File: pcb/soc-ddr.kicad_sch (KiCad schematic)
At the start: 1 part, among them U1 XC7Z020CLG484

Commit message: hierarchy and cleaning
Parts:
- removed U1: XC7Z020CLG484, Package_BGA:Xilinx_CLG484_CLG485, symbol library:XC7Z020CLG484
- added U1: XC7Z020CLG484, Package_BGA:Xilinx_CLG484_CLG485, symbol library:XC7Z020CLG484

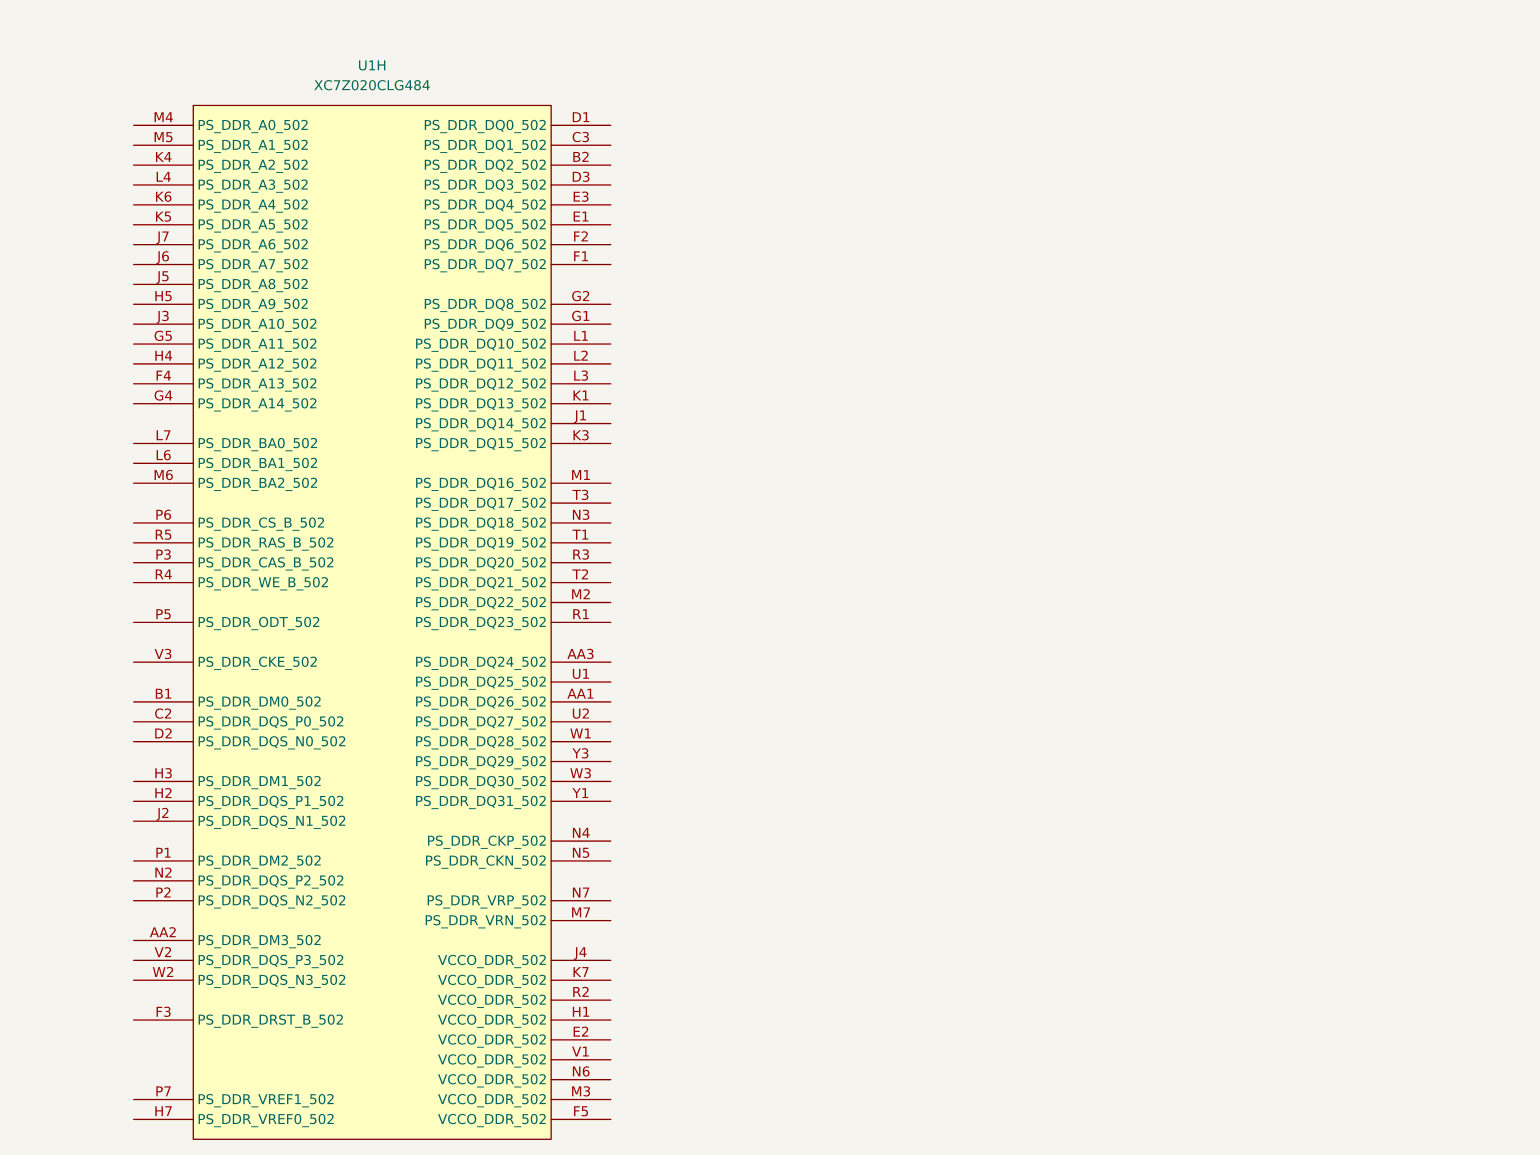
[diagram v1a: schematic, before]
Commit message: schematic structure, added qspi flash, pinout defs. mostly work on PS pinouts, defining comms. buses, still need to choose dram part, phys, camera/bus, power supply etc
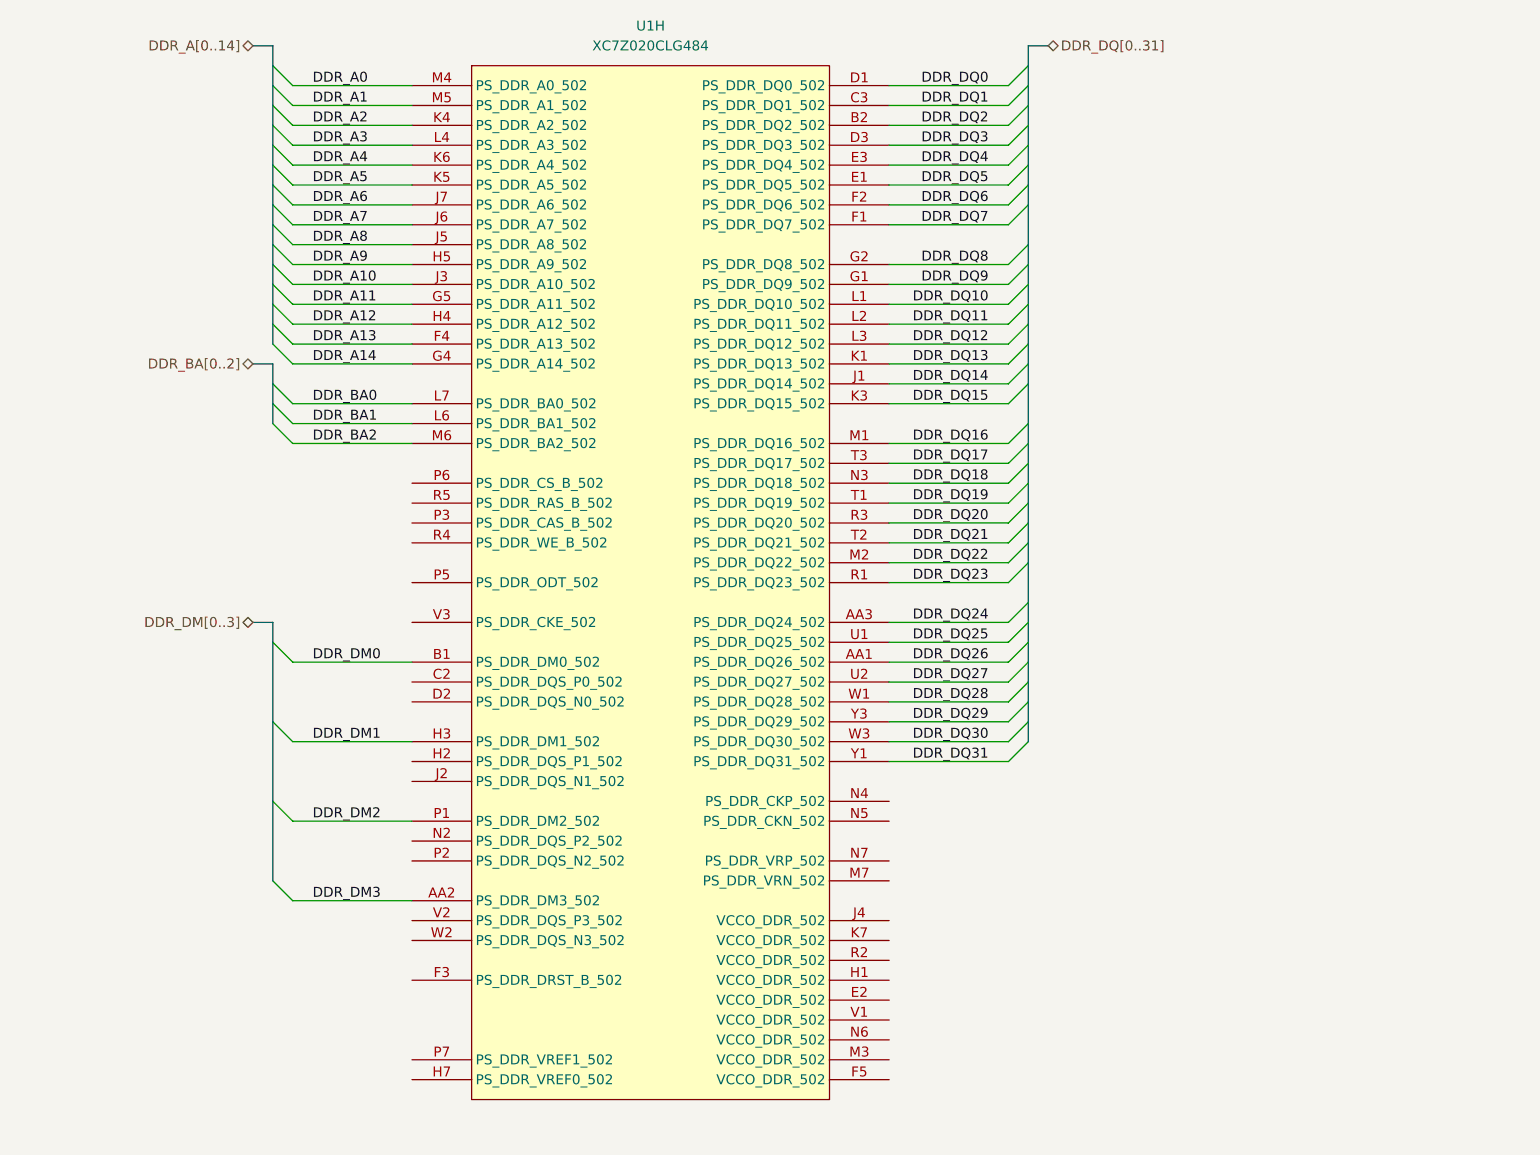
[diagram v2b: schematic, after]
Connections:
- net DDR_DQ26: now reaches U1.AA1 (PS_DDR_DQ26_502)
- net DDR_DM3: now reaches U1.AA2 (PS_DDR_DM3_502)
- net DDR_DQ24: now reaches U1.AA3 (PS_DDR_DQ24_502)
- net DDR_DM0: now reaches U1.B1 (PS_DDR_DM0_502)
- net DDR_DQ2: now reaches U1.B2 (PS_DDR_DQ2_502)
- net DDR_DQ1: now reaches U1.C3 (PS_DDR_DQ1_502)
- net DDR_DQ0: now reaches U1.D1 (PS_DDR_DQ0_502)
- net DDR_DQ3: now reaches U1.D3 (PS_DDR_DQ3_502)
- net DDR_DQ5: now reaches U1.E1 (PS_DDR_DQ5_502)
- net DDR_DQ4: now reaches U1.E3 (PS_DDR_DQ4_502)
- net DDR_DQ7: now reaches U1.F1 (PS_DDR_DQ7_502)
- net DDR_DQ6: now reaches U1.F2 (PS_DDR_DQ6_502)
- net DDR_A13: now reaches U1.F4 (PS_DDR_A13_502)
- net DDR_DQ9: now reaches U1.G1 (PS_DDR_DQ9_502)
- net DDR_DQ8: now reaches U1.G2 (PS_DDR_DQ8_502)
- net DDR_A14: now reaches U1.G4 (PS_DDR_A14_502)
- net DDR_A11: now reaches U1.G5 (PS_DDR_A11_502)
- net DDR_DM1: now reaches U1.H3 (PS_DDR_DM1_502)
- net DDR_A12: now reaches U1.H4 (PS_DDR_A12_502)
- net DDR_A9: now reaches U1.H5 (PS_DDR_A9_502)
- net DDR_DQ14: now reaches U1.J1 (PS_DDR_DQ14_502)
- net DDR_A10: now reaches U1.J3 (PS_DDR_A10_502)
- net DDR_A8: now reaches U1.J5 (PS_DDR_A8_502)
- net DDR_A7: now reaches U1.J6 (PS_DDR_A7_502)
- net DDR_A6: now reaches U1.J7 (PS_DDR_A6_502)
- net DDR_DQ13: now reaches U1.K1 (PS_DDR_DQ13_502)
- net DDR_DQ15: now reaches U1.K3 (PS_DDR_DQ15_502)
- net DDR_A2: now reaches U1.K4 (PS_DDR_A2_502)
- net DDR_A5: now reaches U1.K5 (PS_DDR_A5_502)
- net DDR_A4: now reaches U1.K6 (PS_DDR_A4_502)
- net DDR_DQ10: now reaches U1.L1 (PS_DDR_DQ10_502)
- net DDR_DQ11: now reaches U1.L2 (PS_DDR_DQ11_502)
- net DDR_DQ12: now reaches U1.L3 (PS_DDR_DQ12_502)
- net DDR_A3: now reaches U1.L4 (PS_DDR_A3_502)
- net DDR_BA1: now reaches U1.L6 (PS_DDR_BA1_502)
- net DDR_BA0: now reaches U1.L7 (PS_DDR_BA0_502)
- net DDR_DQ16: now reaches U1.M1 (PS_DDR_DQ16_502)
- net DDR_DQ22: now reaches U1.M2 (PS_DDR_DQ22_502)
- net DDR_A0: now reaches U1.M4 (PS_DDR_A0_502)
- net DDR_A1: now reaches U1.M5 (PS_DDR_A1_502)
- net DDR_BA2: now reaches U1.M6 (PS_DDR_BA2_502)
- net DDR_DQ18: now reaches U1.N3 (PS_DDR_DQ18_502)
- net DDR_DM2: now reaches U1.P1 (PS_DDR_DM2_502)
- net DDR_DQ23: now reaches U1.R1 (PS_DDR_DQ23_502)
- net DDR_DQ20: now reaches U1.R3 (PS_DDR_DQ20_502)
- net DDR_DQ19: now reaches U1.T1 (PS_DDR_DQ19_502)
- net DDR_DQ21: now reaches U1.T2 (PS_DDR_DQ21_502)
- net DDR_DQ17: now reaches U1.T3 (PS_DDR_DQ17_502)
- net DDR_DQ25: now reaches U1.U1 (PS_DDR_DQ25_502)
- net DDR_DQ27: now reaches U1.U2 (PS_DDR_DQ27_502)
- net DDR_DQ28: now reaches U1.W1 (PS_DDR_DQ28_502)
- net DDR_DQ30: now reaches U1.W3 (PS_DDR_DQ30_502)
- net DDR_DQ31: now reaches U1.Y1 (PS_DDR_DQ31_502)
- net DDR_DQ29: now reaches U1.Y3 (PS_DDR_DQ29_502)
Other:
- title: (none) -> CUTIE-CITRUS
- moved on the sheet: U1H

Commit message: added ddr3l
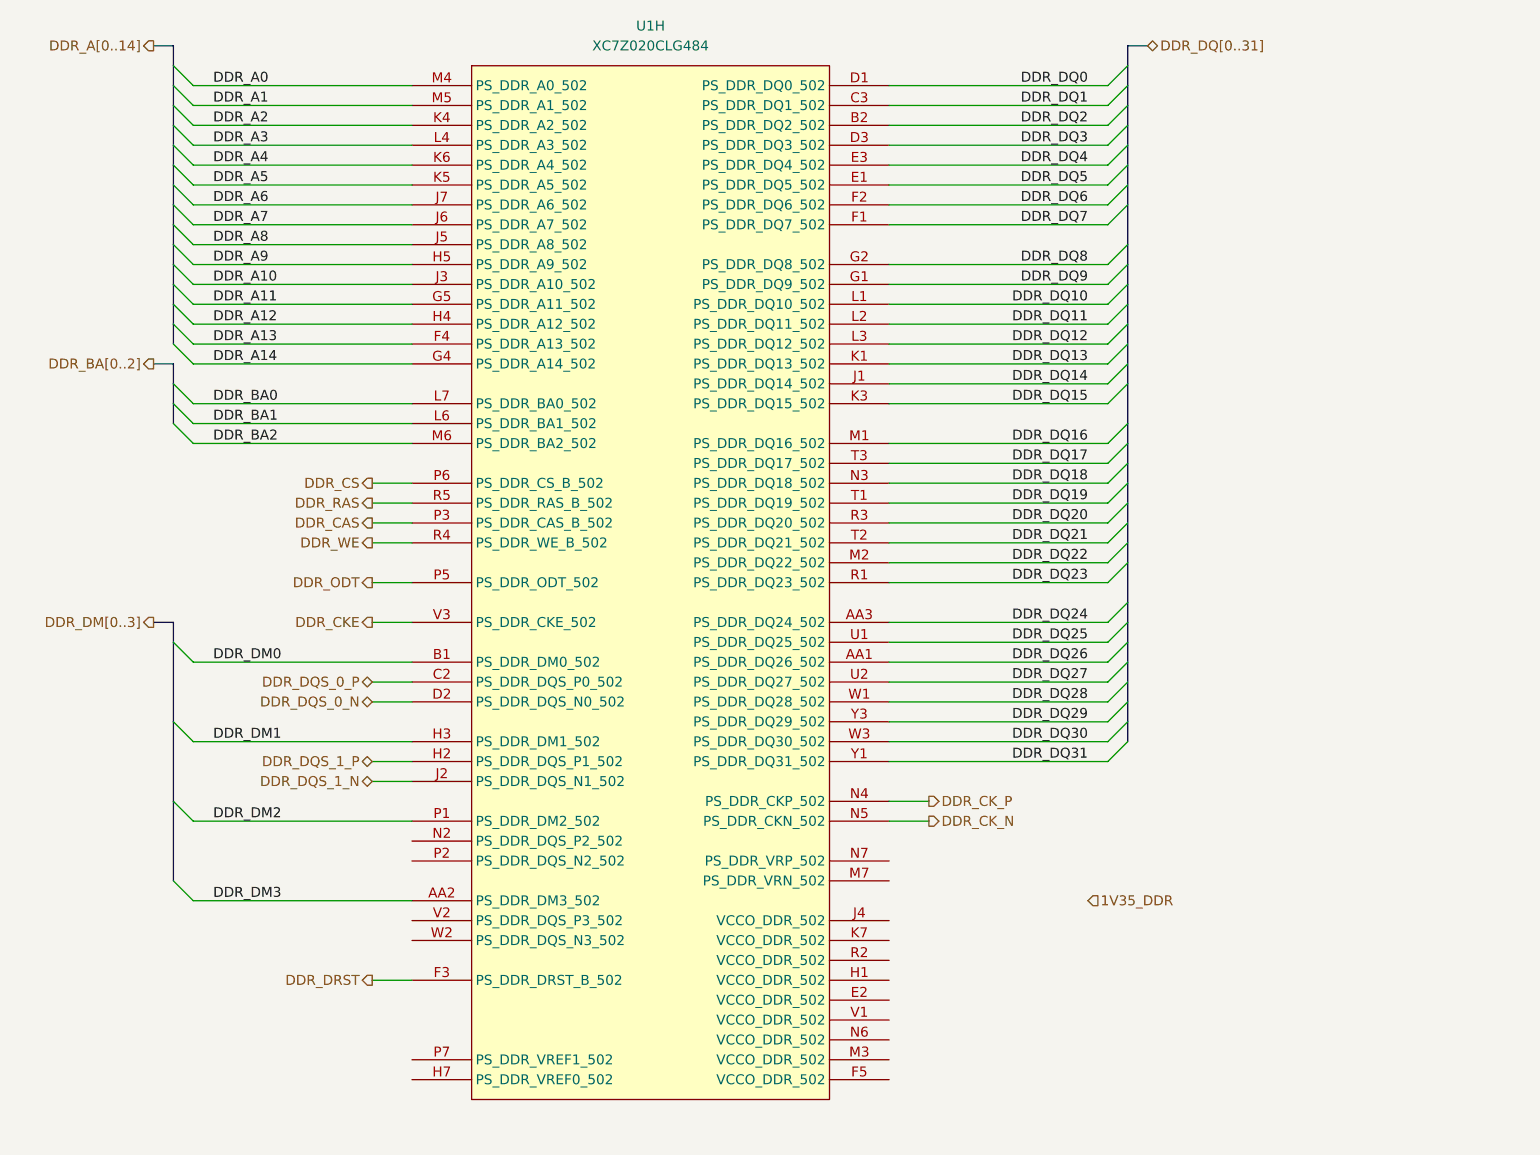
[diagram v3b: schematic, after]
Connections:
- net DDR_DQS_0_P: now reaches U1.C2 (PS_DDR_DQS_P0_502)
- net DDR_DQS_0_N: now reaches U1.D2 (PS_DDR_DQS_N0_502)
- net DDR_DRST: now reaches U1.F3 (PS_DDR_DRST_B_502)
- net DDR_DQS_1_P: now reaches U1.H2 (PS_DDR_DQS_P1_502)
- net DDR_DQS_1_N: now reaches U1.J2 (PS_DDR_DQS_N1_502)
- net DDR_CK_P: now reaches U1.N4 (PS_DDR_CKP_502)
- net DDR_CK_N: now reaches U1.N5 (PS_DDR_CKN_502)
- net DDR_CAS: now reaches U1.P3 (PS_DDR_CAS_B_502)
- net DDR_ODT: now reaches U1.P5 (PS_DDR_ODT_502)
- net DDR_CS: now reaches U1.P6 (PS_DDR_CS_B_502)
- net DDR_WE: now reaches U1.R4 (PS_DDR_WE_B_502)
- net DDR_RAS: now reaches U1.R5 (PS_DDR_RAS_B_502)
- net DDR_CKE: now reaches U1.V3 (PS_DDR_CKE_502)
